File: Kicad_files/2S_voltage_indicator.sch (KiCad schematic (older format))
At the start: 14 parts, among them IC1 LM3916N, U1 YAAJ_DCDC_StepUp_SX1308

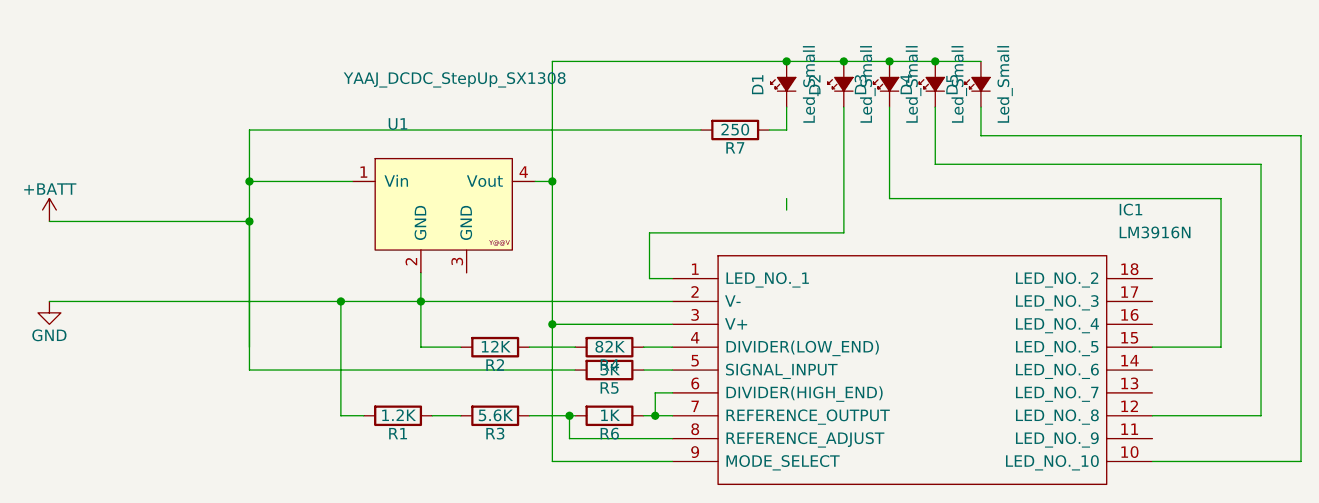
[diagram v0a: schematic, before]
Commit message: voltage adjustments
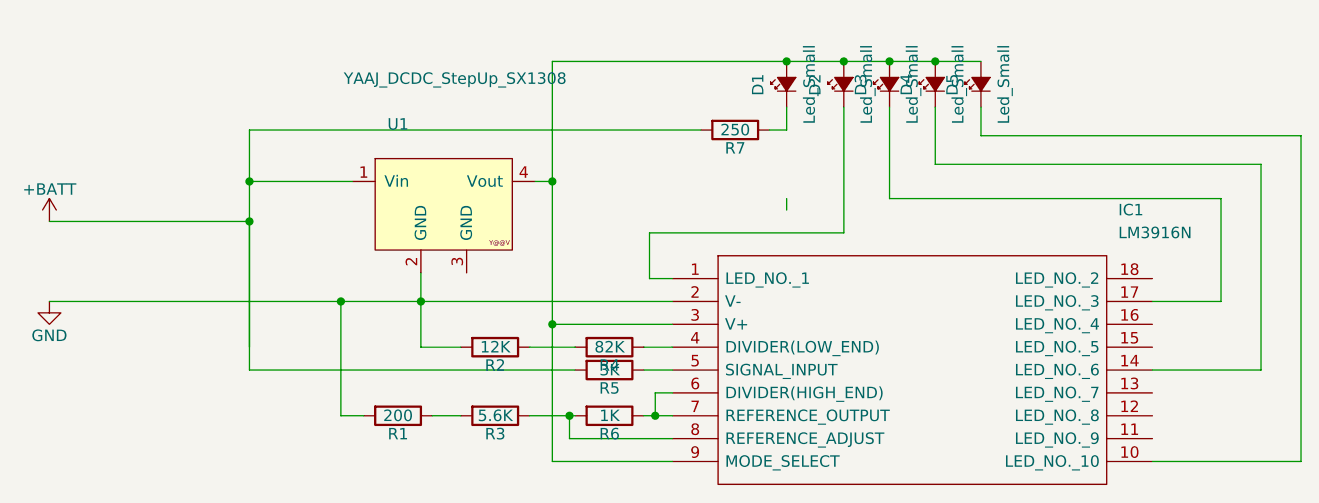
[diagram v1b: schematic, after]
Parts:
- R1: value 1.2K -> 200
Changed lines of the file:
@@
 LIBS:contrib
 LIBS:valves
-LIBS:LM3916N
-LIBS:yaaj_dcdc_stepup_sx1308
+LIBS:2S_voltage_indicator-cache
 EELAYER 25 0
 EELAYER END
@@
 	5650 2400 7075 2400
 Wire Wire Line
-	7075 2400 7075 3500
-Wire Wire Line
-	7075 3500 6600 3500
+	7075 2400 7075 3300
 Wire Wire Line
 	5450 2150 5450 2550
@@
 	5450 2550 6900 2550
 Wire Wire Line
-	6900 2550 6900 3200
-Wire Wire Line
-	6900 3200 6600 3200
+	6900 2550 6900 3000
 Wire Wire Line
 	3975 3700 4500 3700
@@
 P 3300 3500
 F 0 "R1" V 3380 3500 50  0000 C CNN
-F 1 "1.2K" V 3300 3500 50  0000 C CNN
+F 1 "200" V 3300 3500 50  0000 C CNN
 F 2 "" V 3230 3500 50  0000 C CNN
 F 3 "" H 3300 3500 50  0000 C CNN
@@
 	4625 2250 2650 2250
 Connection ~ 2650 2475
+Wire Wire Line
+	6900 3000 6600 3000
+Wire Wire Line
+	7075 3300 6600 3300
 $EndSCHEMATC
